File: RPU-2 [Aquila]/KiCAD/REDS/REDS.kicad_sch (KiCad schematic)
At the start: 13 parts, among them J1 Pigtail, M1 Motor_Servo, U1 MAX4543, U2 AmazonBuck, U3 LM555xN

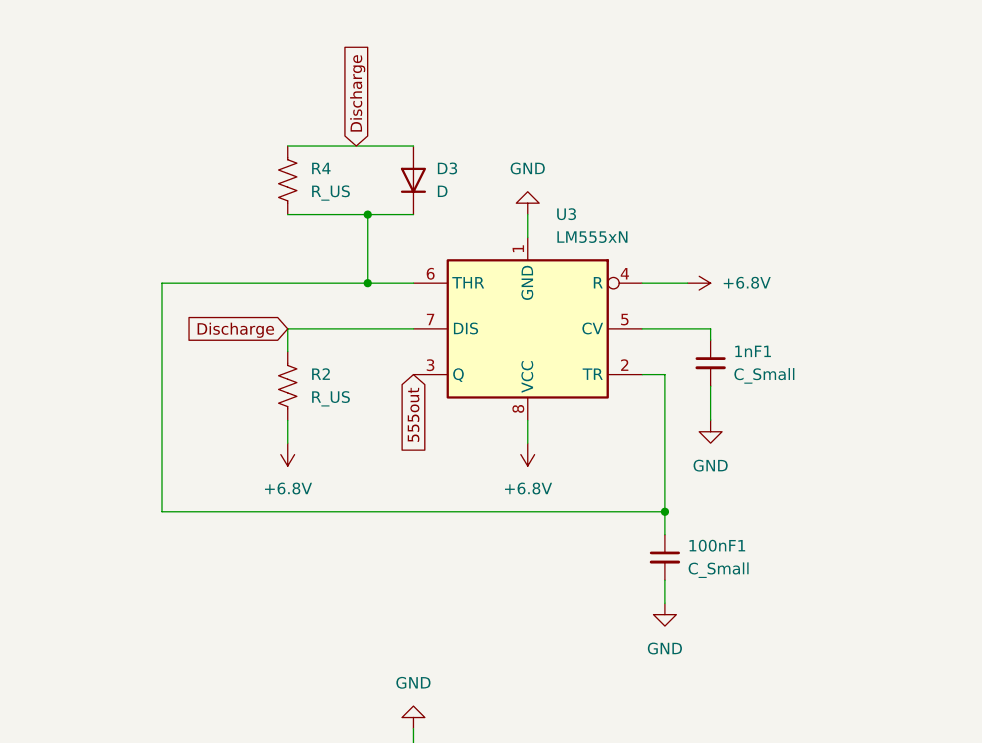
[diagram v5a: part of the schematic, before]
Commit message: update resistor values
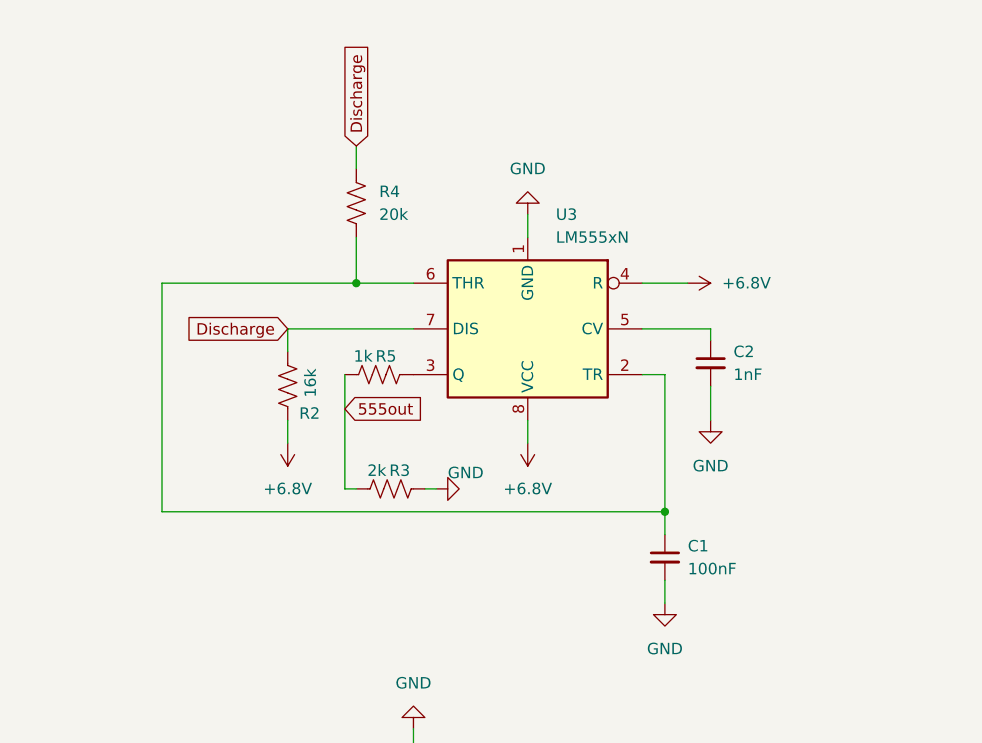
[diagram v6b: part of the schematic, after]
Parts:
- removed D3: D, Diode_THT:D_DO-201_P15.24mm_Horizontal, symbol Device:D
- added R3: 2k, Resistor_THT:R_Axial_DIN0207_L6.3mm_D2.5mm_P10.16mm_Horizontal, symbol Device:R_US
- added R5: 1k, Resistor_THT:R_Axial_DIN0207_L6.3mm_D2.5mm_P10.16mm_Horizontal, symbol Device:R_US
- C1: renamed from 100nF1; value C_Small -> 100nF
- C2: renamed from 1nF1; value C_Small -> 1nF
- D1, D2: footprint Diode_SMD:D_SOD-523 -> Diode_THT:D_DO-201_P12.70mm_Horizontal
- J1: footprint TerminalBlock_WAGO:TerminalBlock_WAGO_804-302_1x02_P7.50mm_45Degree -> Connector_Wire:SolderWire-0.15sqmm_1x02_P4mm_D0.5mm_OD1.5mm
- M1: footprint TerminalBlock_WAGO:TerminalBlock_WAGO_804-303_1x03_P7.50mm_45Degree -> Connector_Wire:SolderWire-0.15sqmm_1x03_P4mm_D0.5mm_OD1.5mm
- R2: value R_US -> 16k
- R4: value R_US -> 20k
- U1: footprint Package_SO:MSOP-8_3x3mm_P0.65mm -> Package_DIP:DIP-8_W7.62mm
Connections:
- net 555out: now also R3.1, R5.1; no longer U3.3 (Q)
- net GND: now also R3.2
- new net: R5.2, U3.3 (Q)
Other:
- moved on the sheet: R4

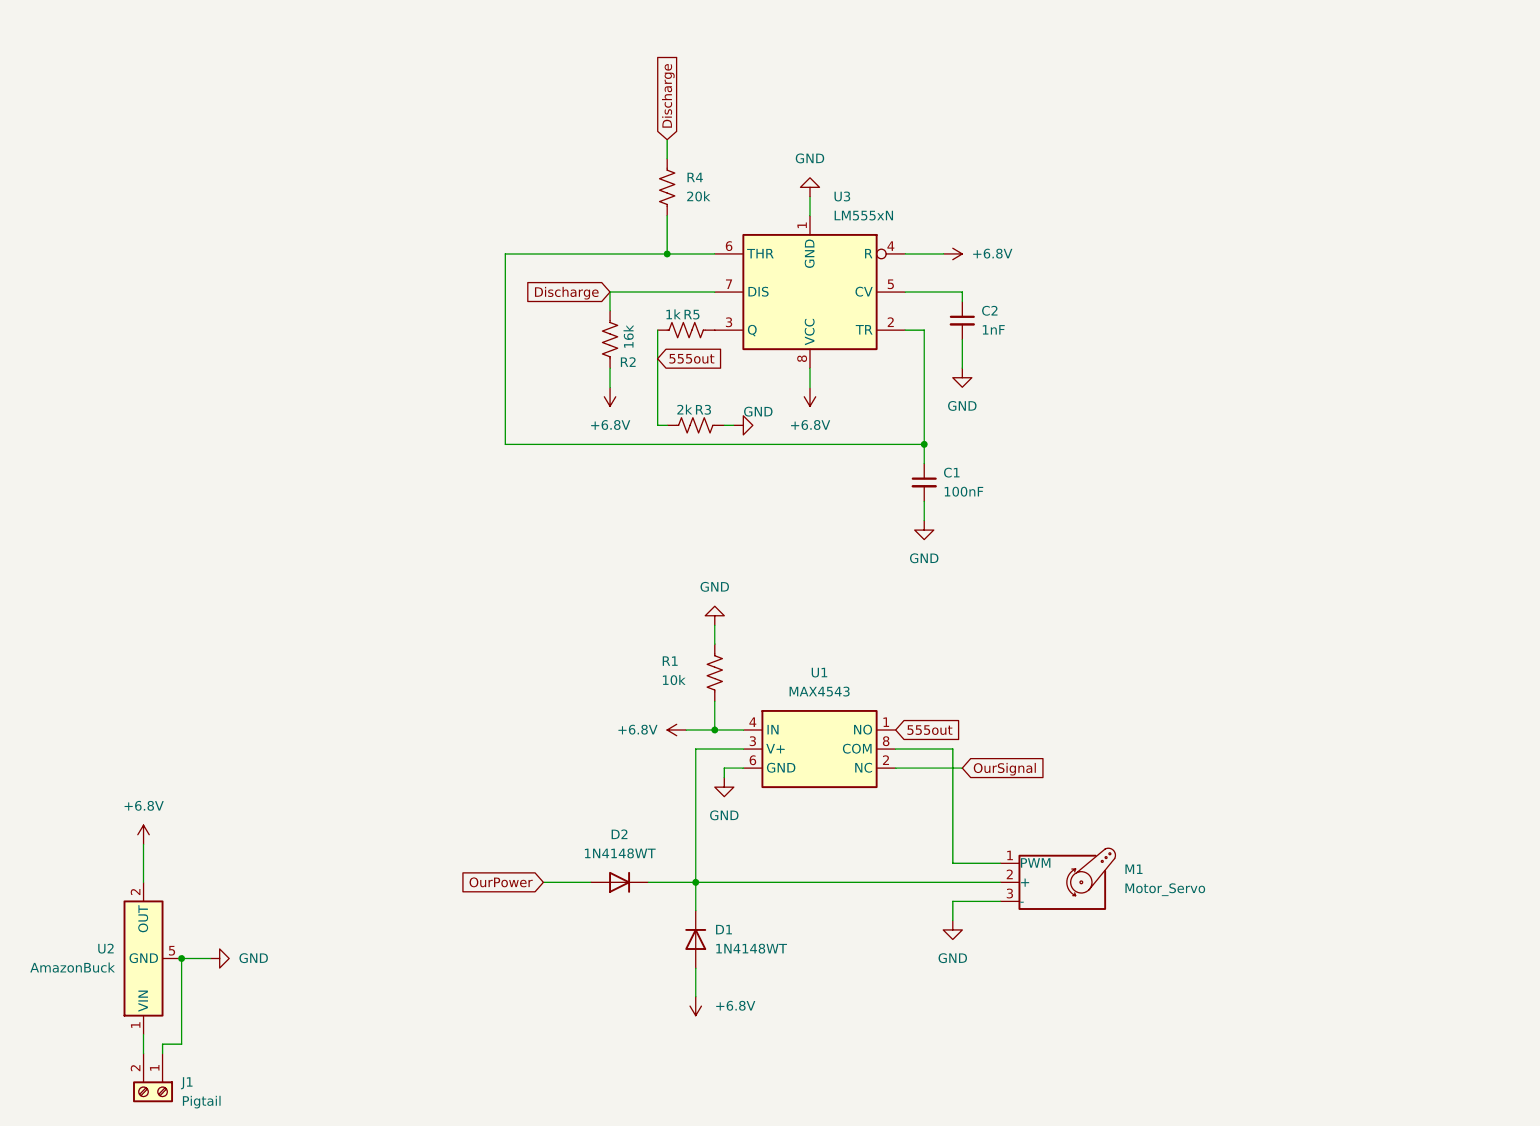
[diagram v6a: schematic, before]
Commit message: updated kicad schematic
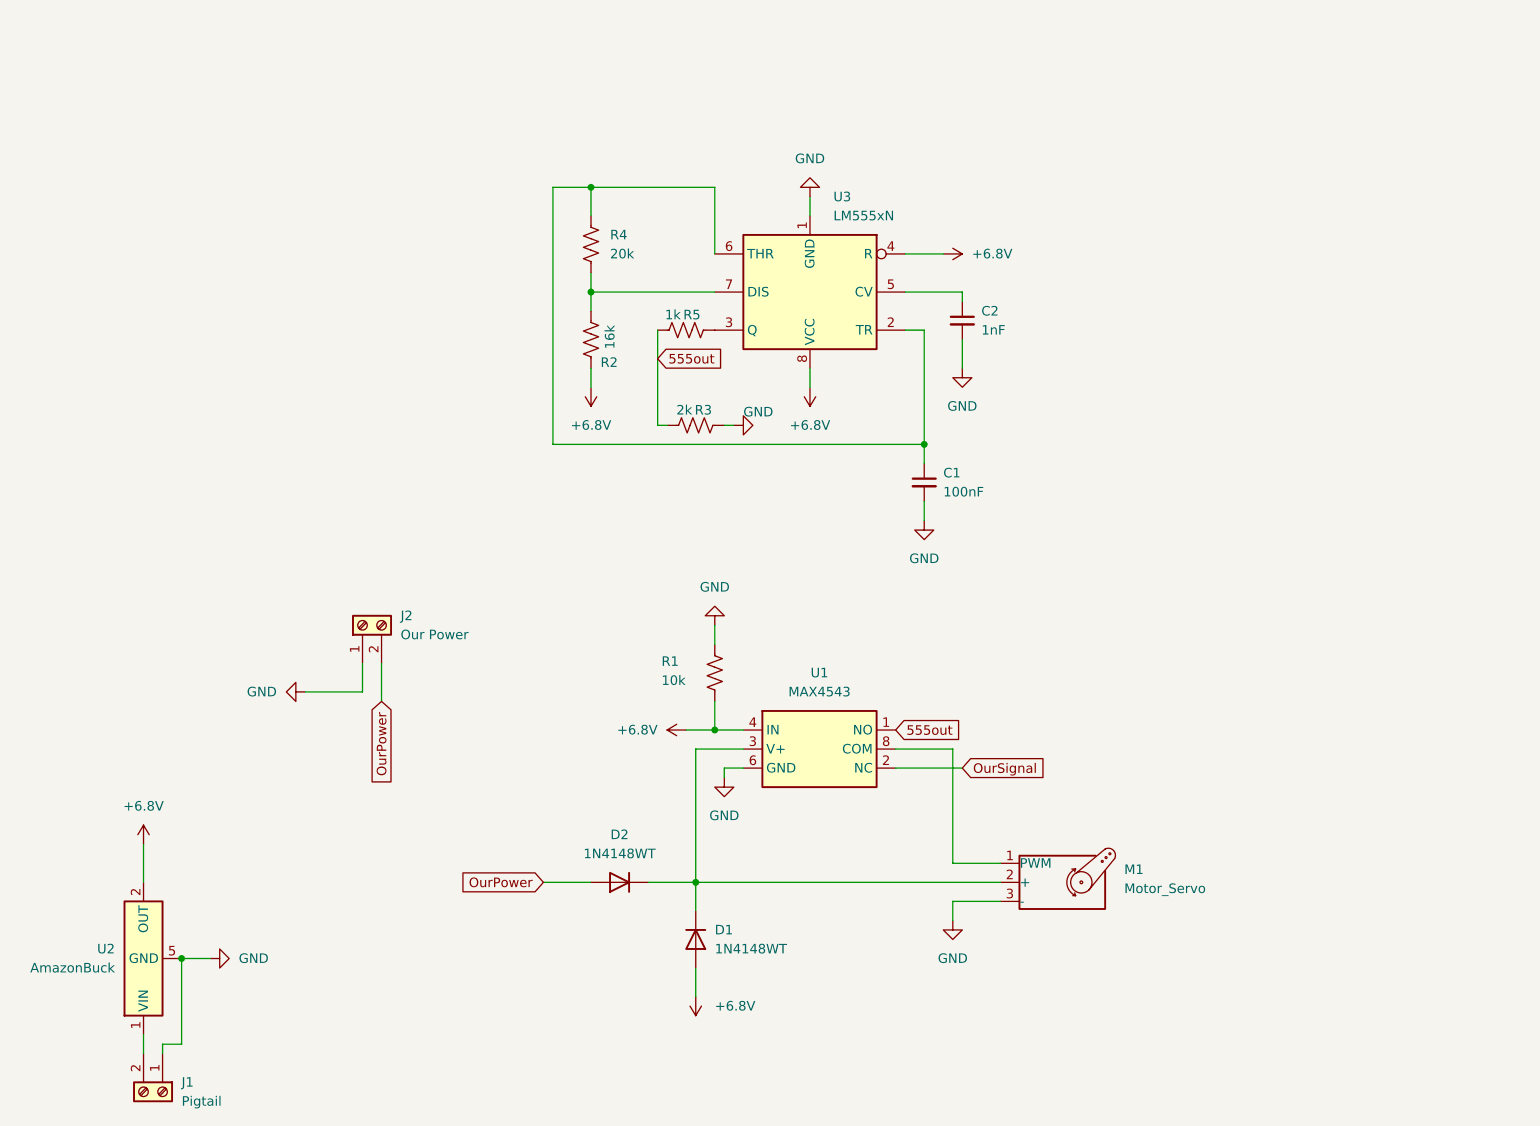
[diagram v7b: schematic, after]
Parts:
- added J2: Our Power, Connector_Wire:SolderWire-0.15sqmm_1x02_P4mm_D0.5mm_OD1.5mm, symbol Connector:Screw_Terminal_01x02
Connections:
- net GND: now also J2.1 (Pin_1)
- net OurPower: now also J2.2 (Pin_2)
- net Discharge: no longer names the net of R2.2, R4.1, U3.7 (DIS)
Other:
- moved on the sheet: R2, R4

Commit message: kicad updat
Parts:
- removed U1: MAX4543, Package_DIP:DIP-8_W7.62mm, symbol MAX4543:MAX4543
- added U4: MAX4544, Package_SO:MSOP-8_3x3mm_P0.65mm, symbol MAX4543:MAX4543
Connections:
- net +6.8V: now also U4.7 (IN)
- net 555out: now also U4.1 (NO)
- net GND: now also U4.4 (GND)
- net OurSignal: now also U4.3 (NC)
- net at D1.1 (K), D2.1 (K), M1.2 (+): now also U4.8 (V+)
- net at M1.1 (PWM): now also U4.2 (COM)
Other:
- moved on the sheet: R1
